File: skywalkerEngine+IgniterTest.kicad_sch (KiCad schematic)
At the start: 49 parts

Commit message: fuckup 2
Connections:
- net at PT?.: now also Engine?.
- net at Engine?.: now also PT?.; no longer PT?.
- net at CV?.: now also Hose?.1; no longer nO_Sol?.
- net at MB_V?.: now also CV?., Fuel?., Hose?.1
- net at QD?.: now also CV?.
- net at CV?.: now also Ox?.; no longer QD?.
- net at PT?.: now also CV?., N?., Reg?., Reg?.
- net at PT?.: no longer Engine?.
- new net: Burst_Disc?., CV?., Fuel?., PT?., SPRV?., nO_Sol?.
- new net: Ox?., PT?., nO_Sol?.
- new net: CV?., nO_Sol?.
- new net: CV?., PT?., Reg?.
- new net: CV?., Fuel?., MB_V?.
- new net: BV?., BV?., Engine?.
- new net: BV?., Burst_Disc?., CV?., Ox?., PT?., SPRV?.
- new net: BV?., Reg?., nO_Sol?.
- now unconnected: Burst_Disc?., Burst_Disc?., N?., PT?., PT?., PT?., PT?.
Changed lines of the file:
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@@
 	)
 	(symbol
-		(lib_name "PID_symbols:Pressure_Transducer")
 		(lib_id "PID_symbols:Pressure_Transducer")
 		(at 49.53 151.13 0)
@@
 	)
 	(symbol
-		(lib_name "PID_symbols:Solenoid")
 		(lib_id "PID_symbols:Solenoid")
 		(at 46.99 87.63 90)
@@
 	)
 	(symbol
-		(lib_name "PID_symbols:Tank")
 		(lib_id "PID_symbols:Tank")
 		(at 118.11 148.59 0)
@@
 	)
 	(symbol
-		(lib_name "PID_symbols:Burst_Disc")
 		(lib_id "PID_symbols:Burst_Disc")
 		(at 36.83 68.58 0)
@@
 	)
 	(symbol
-		(lib_name "PID_symbols:Check_Valve")
 		(lib_id "PID_symbols:Check_Valve")
 		(at 101.6 167.64 270)
@@
 	)
 	(symbol
-		(lib_name "PID_symbols:Check_Valve")
 		(lib_id "PID_symbols:Check_Valve")
 		(at 95.25 125.73 270)
@@
 	)
 	(symbol
-		(lib_name "PID_symbols:Ball_Valve")
 		(lib_id "PID_symbols:Ball_Valve")
 		(at 68.58 138.43 270)
@@
 	)
 	(symbol
-		(lib_name "PID_symbols:Pressure_Transducer")
 		(lib_id "PID_symbols:Pressure_Transducer")
 		(at 73.66 158.75 0)
@@
 	)
 	(symbol
-		(lib_name "PID_symbols:MBallValve")
 		(lib_id "PID_symbols:MBallValve")
 		(at 81.28 179.07 0)
@@
 	)
 	(symbol
-		(lib_name "PID_symbols:Check_Valve")
 		(lib_id "PID_symbols:Check_Valve")
 		(at 68.58 69.85 270)
@@
 	)
 	(symbol
-		(lib_name "PID_symbols:Pressure_Transducer")
 		(lib_id "PID_symbols:Pressure_Transducer")
 		(at 143.51 90.17 0)
@@
 	)
 	(symbol
-		(lib_name "PID_symbols:Solenoid")
 		(lib_id "PID_symbols:Solenoid")
 		(at 76.2 83.82 0)
@@
 	)
 	(symbol
-		(lib_name "PID_symbols:MBallValve")
 		(lib_id "PID_symbols:MBallValve")
 		(at 54.61 109.22 0)
@@
 	)
 	(symbol
-		(lib_name "PID_symbols:Solenoid")
 		(lib_id "PID_symbols:Solenoid")
 		(at 101.6 162.56 90)
@@
 	)
 	(symbol
-		(lib_name "PID_symbols:Quick_Disconnect")
 		(lib_id "PID_symbols:Quick_Disconnect")
 		(at 148.59 157.48 90)
@@
 	)
 	(symbol
-		(lib_name "PID_symbols:Pressure_Transducer")
 		(lib_id "PID_symbols:Pressure_Transducer")
 		(at 87.63 72.39 0)
@@
 	)
 	(symbol
-		(lib_name "PID_symbols:Solenoid")
 		(lib_id "PID_symbols:Solenoid")
 		(at 88.9 54.61 0)
@@
 	)
 	(symbol
-		(lib_name "PID_symbols:Check_Valve")
 		(lib_id "PID_symbols:Check_Valve")
 		(at 82.55 102.87 180)
@@
 	)
 	(symbol
-		(lib_name "PID_symbols:Pressure_Transducer")
 		(lib_id "PID_symbols:Pressure_Transducer")
 		(at 125.73 133.35 0)
@@
 	)
 	(symbol
-		(lib_name "PID_symbols:Pressure_Transducer")
 		(lib_id "PID_symbols:Pressure_Transducer")
 		(at 55.88 38.1 0)
@@
 	)
 	(symbol
-		(lib_name "PID_symbols:Check_Valve")
 		(lib_id "PID_symbols:Check_Valve")
 		(at 148.59 151.13 90)
@@
 	)
 	(symbol
-		(lib_name "PID_symbols:Pressure_Transducer")
 		(lib_id "PID_symbols:Pressure_Transducer")
 		(at 54.61 85.09 0)
@@
 	)
 	(symbol
-		(lib_name "PID_symbols:Tank")
 		(lib_id "PID_symbols:Tank")
 		(at 67.31 99.06 0)
@@
 	)
 	(symbol
-		(lib_name "PID_symbols:Check_Valve")
 		(lib_id "PID_symbols:Check_Valve")
 		(at 60.96 69.85 270)
@@
 	)
 	(symbol
-		(lib_name "PID_symbols:Pressure_Regulator")
 		(lib_id "PID_symbols:Pressure_Regulator")
 		(at 64.77 52.07 90)
@@
 	)
 	(symbol
-		(lib_name "PID_symbols:Tank")
 		(lib_id "PID_symbols:Tank")
 		(at 59.69 99.06 0)
@@
 	)
 	(symbol
-		(lib_name "PID_symbols:SPRV")
 		(lib_id "PID_symbols:SPRV")
 		(at 114.3 77.47 0)
@@
 	)
 	(symbol
-		(lib_name "PID_symbols:SPRV")
 		(lib_id "PID_symbols:SPRV")
 		(at 21.59 77.47 0)
@@
 	)
 	(symbol
-		(lib_name "PID_symbols:Pressure_Transducer")
 		(lib_id "PID_symbols:Pressure_Transducer")
 		(at 78.74 151.13 0)
@@
 	)
 	(symbol
-		(lib_name "PID_symbols:Check_Valve")
 		(lib_id "PID_symbols:Check_Valve")
 		(at 106.68 26.67 180)
@@
 	)
 	(symbol
-		(lib_name "PID_symbols:Quick_Disconnect")
 		(lib_id "PID_symbols:Quick_Disconnect")
 		(at 55.88 179.07 0)
@@
 	)
 	(symbol
-		(lib_name "PID_symbols:Ball_Valve")
 		(lib_id "PID_symbols:Ball_Valve")
 		(at 60.96 138.43 270)
@@
 	)
 	(symbol
-		(lib_name "PID_symbols:Tank")
 		(lib_id "PID_symbols:Tank")
 		(at 93.98 148.59 0)
@@
 	)
 	(symbol
-		(lib_name "PID_symbols:Pressure_Regulator")
 		(lib_id "PID_symbols:Pressure_Regulator")
 		(at 82.55 38.1 0)
@@
 	)
 	(symbol
-		(lib_name "PID_symbols:Check_Valve")
 		(lib_id "PID_symbols:Check_Valve")
 		(at 111.76 167.64 270)
@@
 	)
 	(symbol
-		(lib_name "PID_symbols:Burst_Disc")
 		(lib_id "PID_symbols:Burst_Disc")
 		(at 96.52 69.85 0)
@@
 	)
 	(symbol
-		(lib_name "PID_symbols:Ball_Valve")
 		(lib_id "PID_symbols:Ball_Valve")
 		(at 64.77 64.77 90)
@@
 	)
 	(symbol
-		(lib_name "PID_symbols:Tank")
 		(lib_id "PID_symbols:Tank")
 		(at 63.5 31.75 0)
@@
 	)
 	(symbol
-		(lib_name "PID_symbols:Pressure_Transducer")
 		(lib_id "PID_symbols:Pressure_Transducer")
 		(at 106.68 179.07 0)
@@
 	)
 	(symbol
-		(lib_name "PID_symbols:Ball_Valve")
 		(lib_id "PID_symbols:Ball_Valve")
 		(at 109.22 74.93 90)
@@
 	)
 	(symbol
-		(lib_name "PID_symbols:MBallValve")
 		(lib_id "PID_symbols:MBallValve")
 		(at 102.87 134.62 0)
@@
 	)
 	(symbol
-		(lib_name "PID_symbols:Quick_Disconnect")
 		(lib_id "PID_symbols:Quick_Disconnect")
 		(at 173.99 157.48 90)

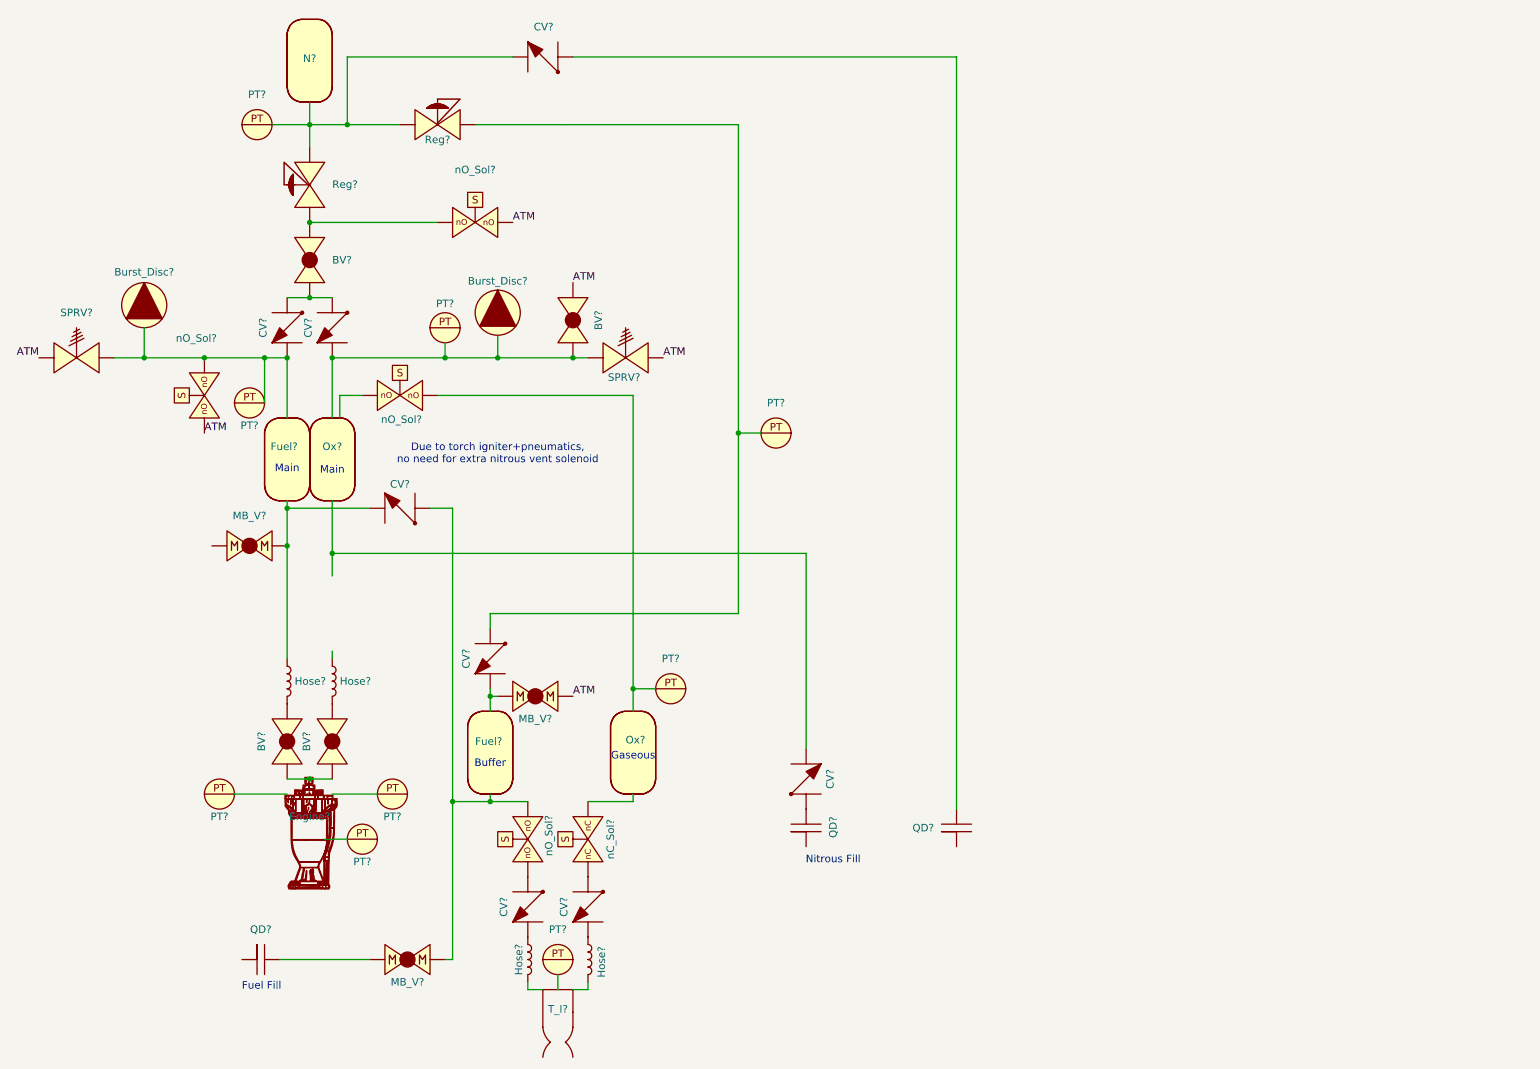
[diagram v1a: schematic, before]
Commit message: Added Igniter + Hopper Engine test
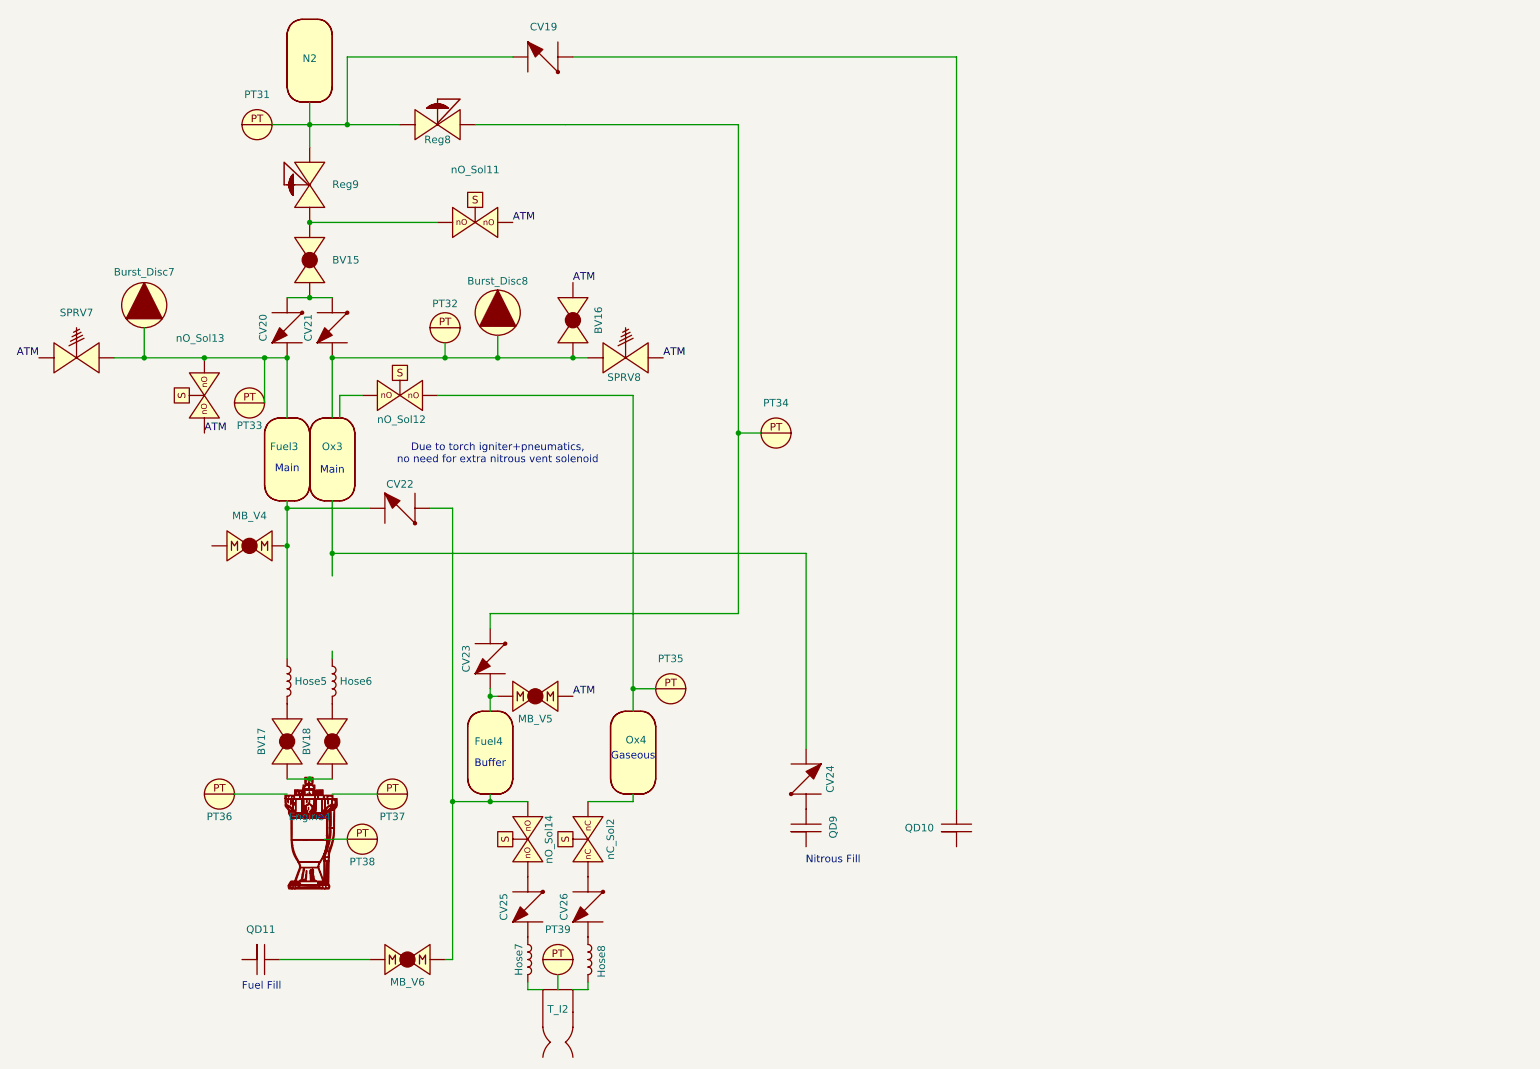
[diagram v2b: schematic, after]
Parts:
- gave numbers to parts that had none: 49
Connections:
- net at PT36.: now also Engine4.
- net at Engine4.: now also PT37.; no longer PT36.
- net at CV25.: now also Hose7.1; no longer nO_Sol14.
- net at MB_V4.: now also CV22., Fuel3., Hose5.1
- net at QD9.: now also CV24.
- net at CV24.: now also Ox3.; no longer QD9.
- net at PT31.: now also CV19., N2., Reg8., Reg9.
- net at PT37.: no longer Engine4.
- new net: Burst_Disc7., CV20., Fuel3., PT33., SPRV7., nO_Sol13.
- new net: Ox4., PT35., nO_Sol12.
- new net: CV25., nO_Sol14.
- new net: CV23., PT34., Reg8.
- new net: CV23., Fuel4., MB_V5.
- new net: BV17., BV18., Engine4.
- new net: BV16., Burst_Disc8., CV21., Ox3., PT32., SPRV8.
- new net: BV15., Reg9., nO_Sol11.
- now unconnected: Burst_Disc7., Burst_Disc8., N2., PT32., PT33., PT34., PT35.
